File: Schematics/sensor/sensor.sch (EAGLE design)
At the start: 9 parts

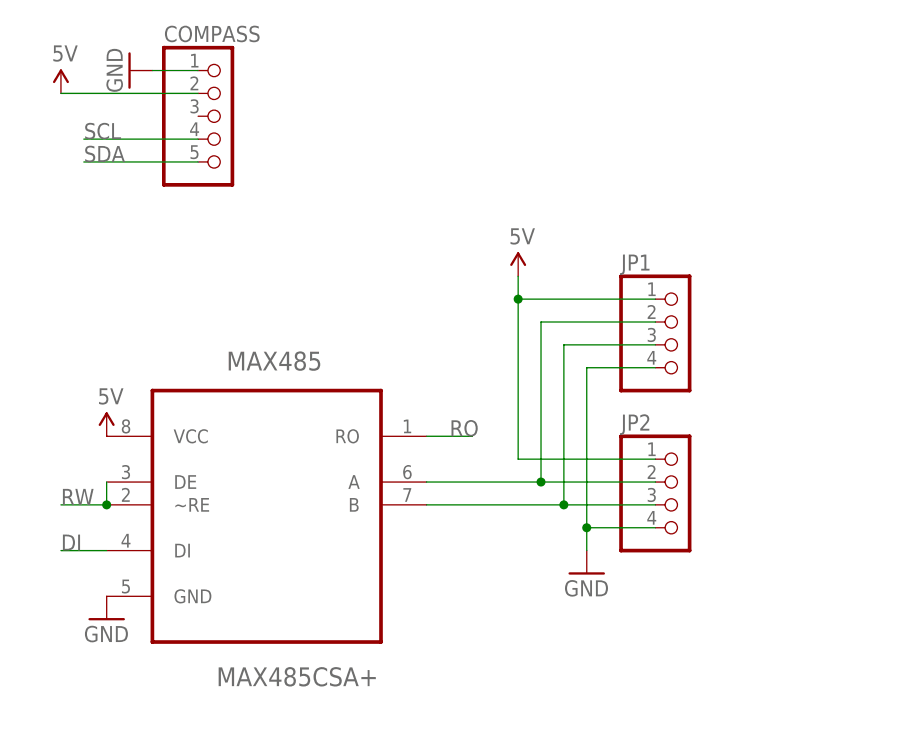
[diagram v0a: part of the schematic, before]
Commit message: Changed headers for 485 bus and added more labels.
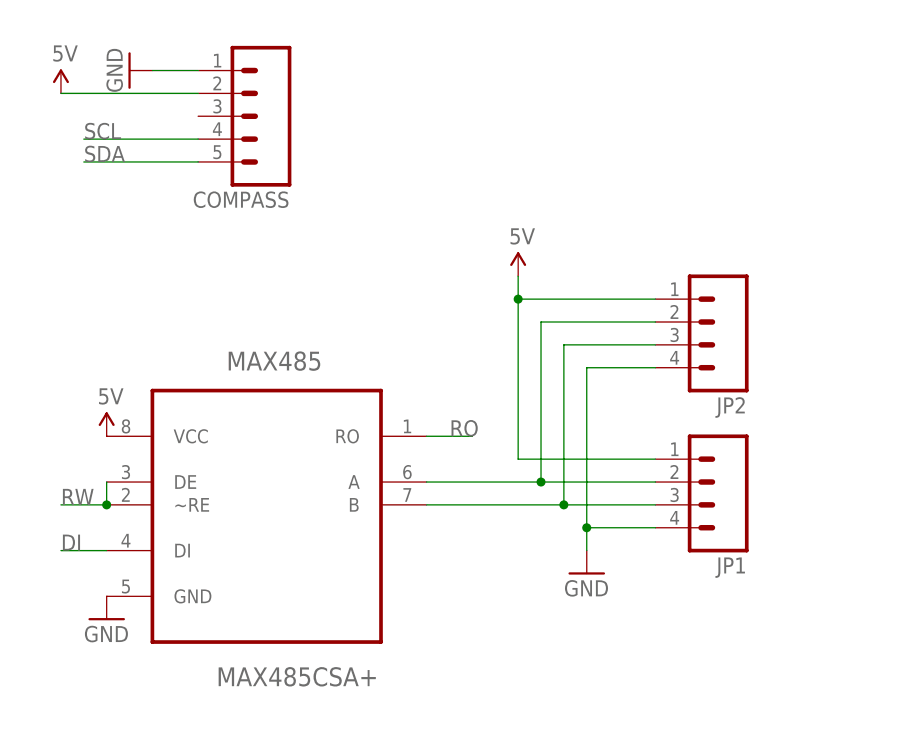
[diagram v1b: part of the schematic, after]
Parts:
- COMPASS: device pinhead:PINHD-1X5 -> SparkFun-Connectors:M05PTH
- JP1, JP2: device pinhead:PINHD-1X4 -> SparkFun-Connectors:M04PTH
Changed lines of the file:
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@@
 <part name="MAX485" library="Maxim_By_element14_Batch_1" deviceset="MAX485CSA+" device=""/>
 <part name="ISP" library="adafruit" deviceset="AVRISP" device="-6"/>
-<part name="JP1" library="pinhead" deviceset="PINHD-1X4" device=""/>
-<part name="JP2" library="pinhead" deviceset="PINHD-1X4" device=""/>
-<part name="COMPASS" library="pinhead" deviceset="PINHD-1X5" device=""/>
 <part name="Y1" library="SparkFun-FreqCtrl" deviceset="RESONATOR" device="PTH"/>
 <part name="GND1" library="SparkFun-Aesthetics" deviceset="GND" device=""/>
@@
 <part name="GND7" library="SparkFun-Aesthetics" deviceset="GND" device=""/>
 <part name="R1" library="SparkFun-Passives" deviceset="RESISTOR" device="1206" value="10K"/>
+<part name="JP1" library="SparkFun-Connectors" deviceset="M04" device="PTH"/>
+<part name="JP2" library="SparkFun-Connectors" deviceset="M04" device="PTH"/>
+<part name="COMPASS" library="SparkFun-Connectors" deviceset="M05" device="PTH"/>
 </parts>
 <sheets>
@@
 <instance part="MAX485" gate="A" x="165.1" y="111.76"/>
 <instance part="ISP" gate="G$1" x="104.14" y="60.96"/>
-<instance part="JP1" gate="A" x="210.82" y="127"/>
-<instance part="JP2" gate="A" x="210.82" y="109.22"/>
-<instance part="COMPASS" gate="A" x="160.02" y="152.4"/>
 <instance part="Y1" gate="G$1" x="22.86" y="91.44" rot="R270"/>
 <instance part="GND1" gate="1" x="15.24" y="86.36"/>
@@
 <instance part="GND7" gate="1" x="91.44" y="104.14"/>
 <instance part="R1" gate="G$1" x="22.86" y="127" rot="R90"/>
+<instance part="JP1" gate="G$1" x="213.36" y="111.76" rot="R180"/>
+<instance part="JP2" gate="G$1" x="213.36" y="129.54" rot="R180"/>
+<instance part="COMPASS" gate="G$1" x="165.1" y="152.4" rot="R180"/>
 </instances>
 <busses>
@@
 <segment>
 <pinref part="GND5" gate="1" pin="GND"/>
-<pinref part="COMPASS" gate="A" pin="1"/>
 <wire x1="152.4" y1="157.48" x2="157.48" y2="157.48" width="0.1524" layer="91"/>
-</segment>
-<segment>
-<pinref part="JP2" gate="A" pin="4"/>
+<pinref part="COMPASS" gate="G$1" pin="1"/>
+</segment>
+<segment>
 <pinref part="GND6" gate="1" pin="GND"/>
 <wire x1="208.28" y1="106.68" x2="200.66" y2="106.68" width="0.1524" layer="91"/>
 <wire x1="200.66" y1="106.68" x2="200.66" y2="104.14" width="0.1524" layer="91"/>
-<pinref part="JP1" gate="A" pin="4"/>
 <wire x1="208.28" y1="124.46" x2="200.66" y2="124.46" width="0.1524" layer="91"/>
 <wire x1="200.66" y1="124.46" x2="200.66" y2="106.68" width="0.1524" layer="91"/>
 <junction x="200.66" y="106.68"/>
+<pinref part="JP1" gate="G$1" pin="4"/>
+<pinref part="JP2" gate="G$1" pin="4"/>
 </segment>
 <segment>
@@
 <segment>
 <pinref part="SUPPLY4" gate="G$1" pin="5V"/>
-<pinref part="COMPASS" gate="A" pin="2"/>
 <wire x1="142.24" y1="154.94" x2="157.48" y2="154.94" width="0.1524" layer="91"/>
-</segment>
-<segment>
-<pinref part="JP2" gate="A" pin="1"/>
+<pinref part="COMPASS" gate="G$1" pin="2"/>
+</segment>
+<segment>
 <pinref part="SUPPLY5" gate="G$1" pin="5V"/>
 <wire x1="208.28" y1="114.3" x2="193.04" y2="114.3" width="0.1524" layer="91"/>
 <wire x1="193.04" y1="114.3" x2="193.04" y2="132.08" width="0.1524" layer="91"/>
-<pinref part="JP1" gate="A" pin="1"/>
 <wire x1="193.04" y1="132.08" x2="193.04" y2="134.62" width="0.1524" layer="91"/>
 <wire x1="208.28" y1="132.08" x2="193.04" y2="132.08" width="0.1524" layer="91"/>
 <junction x="193.04" y="132.08"/>
+<pinref part="JP1" gate="G$1" pin="1"/>
+<pinref part="JP2" gate="G$1" pin="1"/>
 </segment>
 <segment>
@@
 <net name="N$7" class="0">
 <segment>
-<pinref part="JP1" gate="A" pin="2"/>
 <wire x1="208.28" y1="129.54" x2="195.58" y2="129.54" width="0.1524" layer="91"/>
 <wire x1="195.58" y1="129.54" x2="195.58" y2="111.76" width="0.1524" layer="91"/>
 <pinref part="MAX485" gate="A" pin="A"/>
 <wire x1="195.58" y1="111.76" x2="182.88" y2="111.76" width="0.1524" layer="91"/>
-<pinref part="JP2" gate="A" pin="2"/>
 <wire x1="208.28" y1="111.76" x2="195.58" y2="111.76" width="0.1524" layer="91"/>
 <junction x="195.58" y="111.76"/>
+<pinref part="JP1" gate="G$1" pin="2"/>
+<pinref part="JP2" gate="G$1" pin="2"/>
 </segment>
 </net>
@@
 <wire x1="182.88" y1="109.22" x2="198.12" y2="109.22" width="0.1524" layer="91"/>
 <wire x1="198.12" y1="109.22" x2="198.12" y2="127" width="0.1524" layer="91"/>
-<pinref part="JP1" gate="A" pin="3"/>
 <wire x1="198.12" y1="127" x2="208.28" y2="127" width="0.1524" layer="91"/>
-<pinref part="JP2" gate="A" pin="3"/>
 <wire x1="208.28" y1="109.22" x2="198.12" y2="109.22" width="0.1524" layer="91"/>
 <junction x="198.12" y="109.22"/>
+<pinref part="JP1" gate="G$1" pin="3"/>
+<pinref part="JP2" gate="G$1" pin="3"/>
 </segment>
 </net>
@@
 <net name="SCL" class="0">
 <segment>
-<pinref part="COMPASS" gate="A" pin="4"/>
 <wire x1="157.48" y1="149.86" x2="144.78" y2="149.86" width="0.1524" layer="91"/>
 <label x="144.78" y="149.86" size="1.778" layer="95"/>
+<pinref part="COMPASS" gate="G$1" pin="4"/>
 </segment>
 <segment>
@@
 <net name="SDA" class="0">
 <segment>
-<pinref part="COMPASS" gate="A" pin="5"/>
 <wire x1="157.48" y1="147.32" x2="144.78" y2="147.32" width="0.1524" layer="91"/>
 <label x="144.78" y="147.32" size="1.778" layer="95"/>
-</segment>
-<segment>
+<pinref part="COMPASS" gate="G$1" pin="5"/>
+</segment>
+<segment>

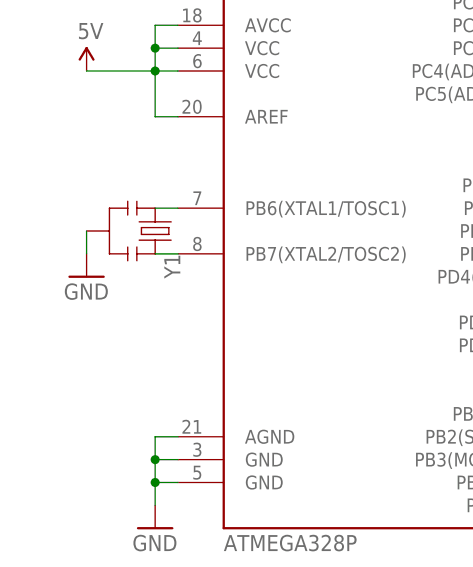
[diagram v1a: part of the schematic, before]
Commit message: Made sensor PCB smaller. Removed through hole circuit.
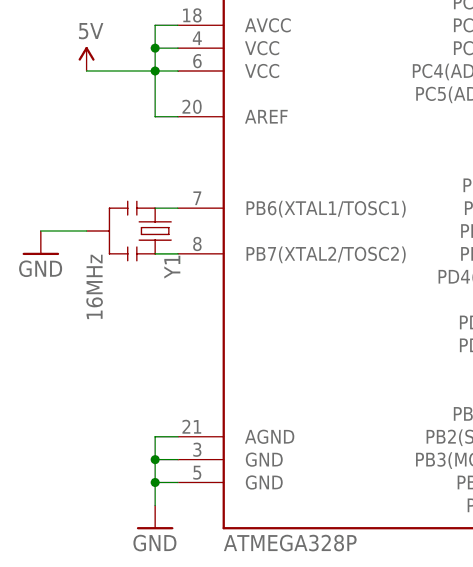
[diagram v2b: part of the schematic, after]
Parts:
- Y1: value (none) -> 16MHz
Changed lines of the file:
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@@
 <part name="MAX485" library="Maxim_By_element14_Batch_1" deviceset="MAX485CSA+" device=""/>
 <part name="ISP" library="adafruit" deviceset="AVRISP" device="-6"/>
-<part name="Y1" library="SparkFun-FreqCtrl" deviceset="RESONATOR" device="PTH"/>
+<part name="Y1" library="SparkFun-FreqCtrl" deviceset="RESONATOR" device="PTH" value="16MHz"/>
 <part name="GND1" library="SparkFun-Aesthetics" deviceset="GND" device=""/>
 <part name="GND2" library="SparkFun-Aesthetics" deviceset="GND" device=""/>
@@
 <instance part="ISP" gate="G$1" x="104.14" y="60.96"/>
 <instance part="Y1" gate="G$1" x="22.86" y="91.44" rot="R270"/>
-<instance part="GND1" gate="1" x="15.24" y="86.36"/>
+<instance part="GND1" gate="1" x="10.16" y="88.9"/>
 <instance part="GND2" gate="1" x="147.32" y="96.52"/>
 <instance part="GND3" gate="1" x="119.38" y="55.88"/>
@@
 <pinref part="Y1" gate="G$1" pin="2"/>
 <pinref part="GND1" gate="1" pin="GND"/>
-<wire x1="15.24" y1="91.44" x2="15.24" y2="88.9" width="0.1524" layer="91"/>
+<wire x1="15.24" y1="91.44" x2="10.16" y2="91.44" width="0.1524" layer="91"/>
 </segment>
 <segment>

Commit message: RX and TX for PROPPLUG weren't connected. they are now.
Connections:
- net N$6: now also ATMEGA328P.PD0(RXD)
- net N$9: now also ATMEGA328P.PD1(TXD)
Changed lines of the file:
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@@
 <pinref part="PROPPLUG" gate="G$1" pin="3"/>
 <wire x1="73.66" y1="96.52" x2="96.52" y2="96.52" width="0.1524" layer="91"/>
+<pinref part="ATMEGA328P" gate="G$1" pin="PD0(RXD)"/>
 </segment>
 </net>
@@
 <pinref part="PROPPLUG" gate="G$1" pin="4"/>
 <wire x1="73.66" y1="93.98" x2="96.52" y2="93.98" width="0.1524" layer="91"/>
+<pinref part="ATMEGA328P" gate="G$1" pin="PD1(TXD)"/>
 </segment>
 </net>

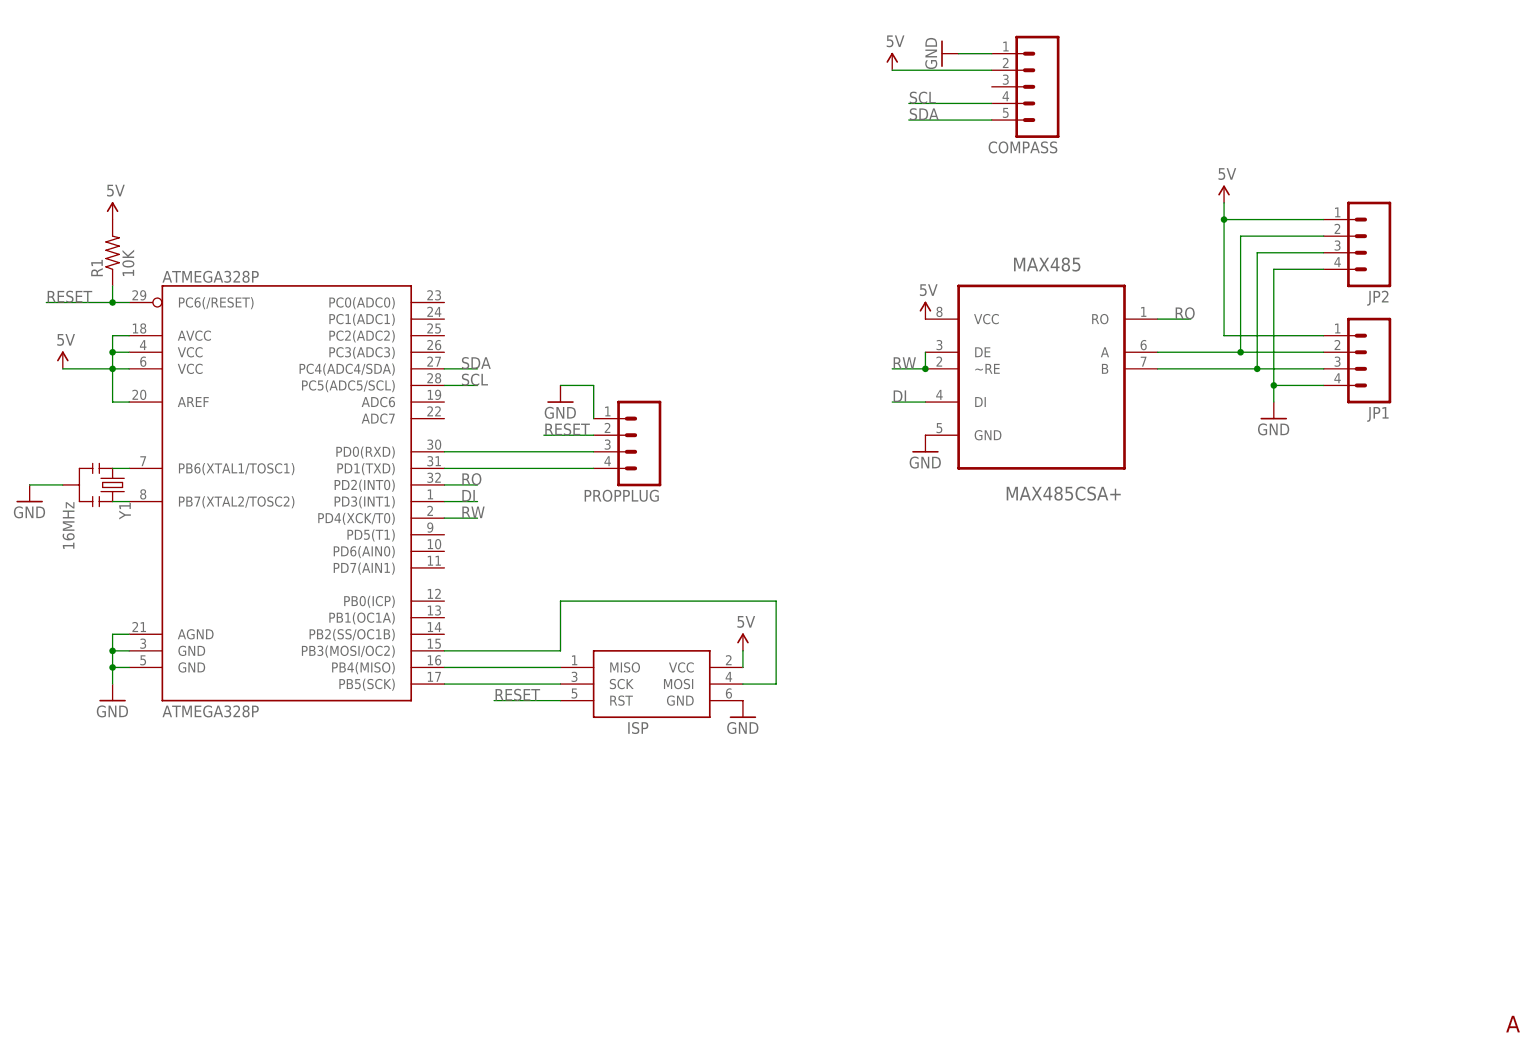
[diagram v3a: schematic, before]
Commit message: Revision by Caleb
Changed programming connectors to be on the surface as pads only for
programming with another board.
Rearranged the board to minimize the size as much as possible.
Dimensions are .95 x .65
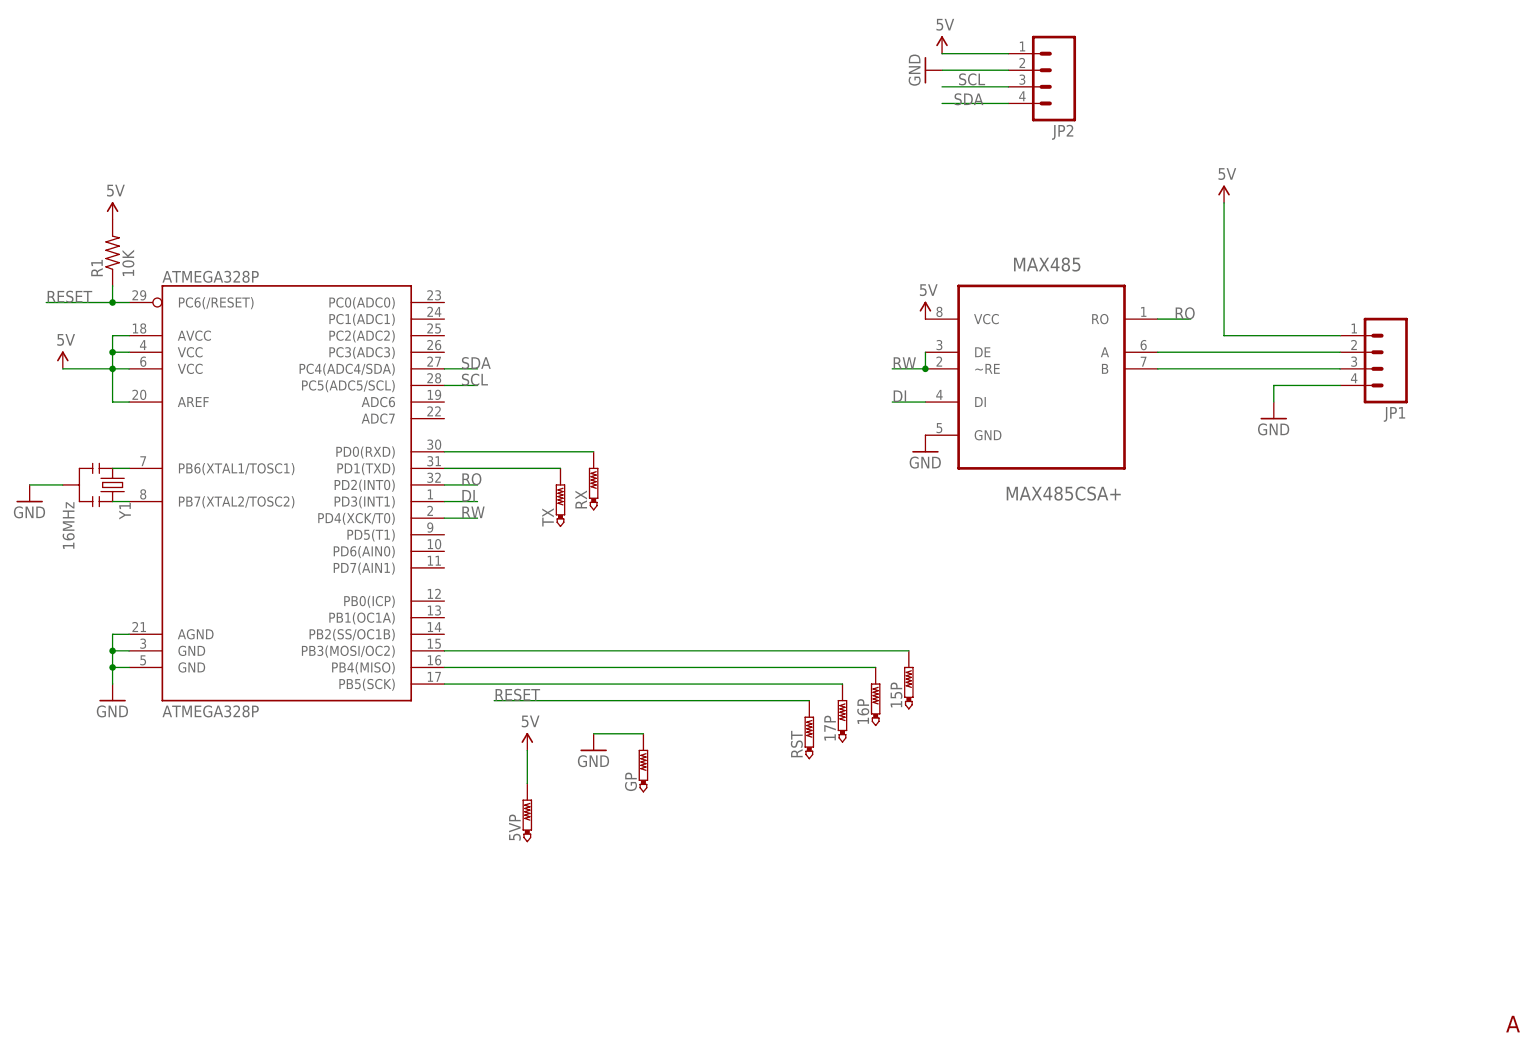
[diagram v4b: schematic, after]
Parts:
- removed COMPASS: (no value), SparkFun-Connectors:M05PTH
- removed ISP: AVRISP-6, adafruit:AVRISP-6
- removed PROPPLUG: (no value), SparkFun-Connectors:M04PTH
- added 15P, 16P, 17P, 5VP, GP, RST, RX, TX: PTR1TP12R, testpad:PTR1TP12R
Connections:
- net 5V: now also 5VP.TP; no longer COMPASS.2, ISP.VCC
- net GND: now also GP.TP, JP2.2; no longer COMPASS.1, ISP.GND, JP2.4, PROPPLUG.1
- net N$3: now also 17P.TP; no longer ISP.SCK
- net N$4: now also 16P.TP; no longer ISP.MISO
- net N$5: now also 15P.TP; no longer ISP.MOSI
- net N$6: now also RX.TP; no longer PROPPLUG.3
- net N$7: no longer JP2.2
- net N$8: no longer JP2.3
- net N$9: now also TX.TP; no longer PROPPLUG.4
- net RESET: now also RST.TP; no longer ISP.RST, PROPPLUG.2
- net SCL: now also JP2.3; no longer COMPASS.4
- net SDA: now also JP2.4; no longer COMPASS.5
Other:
- moved on the sheet: JP1, JP2

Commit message: PCB updates
changed sensor PCB to 3.0
changed Node PCB to 2.0 and parts list to go with it (Sach, can you
look over the schematic, board, and parts list that I have so far to
make sure I have everything correct?)
added Base Station PCB 0.5
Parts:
- removed R1: 10K, SparkFun-Passives:RESISTOR1206
- added PAD1, PAD2: (no value), wirepad:1,6/0,9
- added R2: 10K, SparkFun-Passives:RESISTOR0603-RES
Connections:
- net 5V: now also R2.2; no longer R1.2
- net RESET: now also R2.1; no longer R1.1
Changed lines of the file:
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@@
 <part name="GND6" library="SparkFun-Aesthetics" deviceset="GND" device=""/>
 <part name="SUPPLY6" library="SparkFun-Aesthetics" deviceset="5V" device=""/>
-<part name="R1" library="SparkFun-Passives" deviceset="RESISTOR" device="1206" value="10K"/>
 <part name="15P" library="testpad" deviceset="PTR1" device="TP12R"/>
 <part name="17P" library="testpad" deviceset="PTR1" device="TP12R"/>
@@
 <part name="JP1" library="SparkFun-Connectors" deviceset="M04" device="PTH"/>
 <part name="JP2" library="SparkFun-Connectors" deviceset="M04" device="PTH"/>
+<part name="R2" library="SparkFun-Passives" deviceset="RESISTOR" device="0603-RES" value="10K"/>
+<part name="PAD1" library="wirepad" deviceset="1,6/0,9" device=""/>
+<part name="PAD2" library="wirepad" deviceset="1,6/0,9" device=""/>
 </parts>
 <sheets>
@@
 <instance part="GND6" gate="1" x="200.66" y="101.6"/>
 <instance part="SUPPLY6" gate="G$1" x="22.86" y="132.08"/>
-<instance part="R1" gate="G$1" x="22.86" y="127" rot="R90"/>
 <instance part="15P" gate="G$1" x="144.78" y="63.5"/>
 <instance part="17P" gate="G$1" x="134.62" y="58.42"/>
@@
 <instance part="JP1" gate="G$1" x="215.9" y="111.76" rot="R180"/>
 <instance part="JP2" gate="G$1" x="165.1" y="154.94" rot="R180"/>
+<instance part="R2" gate="G$1" x="22.86" y="127" rot="R90"/>
+<instance part="PAD1" gate="1" x="99.06" y="119.38"/>
+<instance part="PAD2" gate="1" x="88.9" y="127"/>
 </instances>
 <busses>
@@
 </segment>
 <segment>
-<pinref part="SUPPLY6" gate="G$1" pin="5V"/>
-<pinref part="R1" gate="G$1" pin="2"/>
-</segment>
-<segment>
 <wire x1="160.02" y1="157.48" x2="149.86" y2="157.48" width="0.1524" layer="91"/>
 <pinref part="SUPPLY4" gate="G$1" pin="5V"/>
 <pinref part="JP2" gate="G$1" pin="1"/>
+</segment>
+<segment>
+<pinref part="SUPPLY6" gate="G$1" pin="5V"/>
+<pinref part="R2" gate="G$1" pin="2"/>
 </segment>
 </net>
@@
 <wire x1="22.86" y1="121.92" x2="22.86" y2="119.38" width="0.1524" layer="91"/>
 <junction x="22.86" y="119.38"/>
-<pinref part="R1" gate="G$1" pin="1"/>
+<pinref part="R2" gate="G$1" pin="1"/>
 </segment>
 <segment>
